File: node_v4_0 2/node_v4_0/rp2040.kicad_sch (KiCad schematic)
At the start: 29 parts, among them U1 RP2040, U2 W25Q128JVS, U7 PTS526 SK15 SMTR2 LFS, U8 PTS526 SK15 SMTR2 LFS

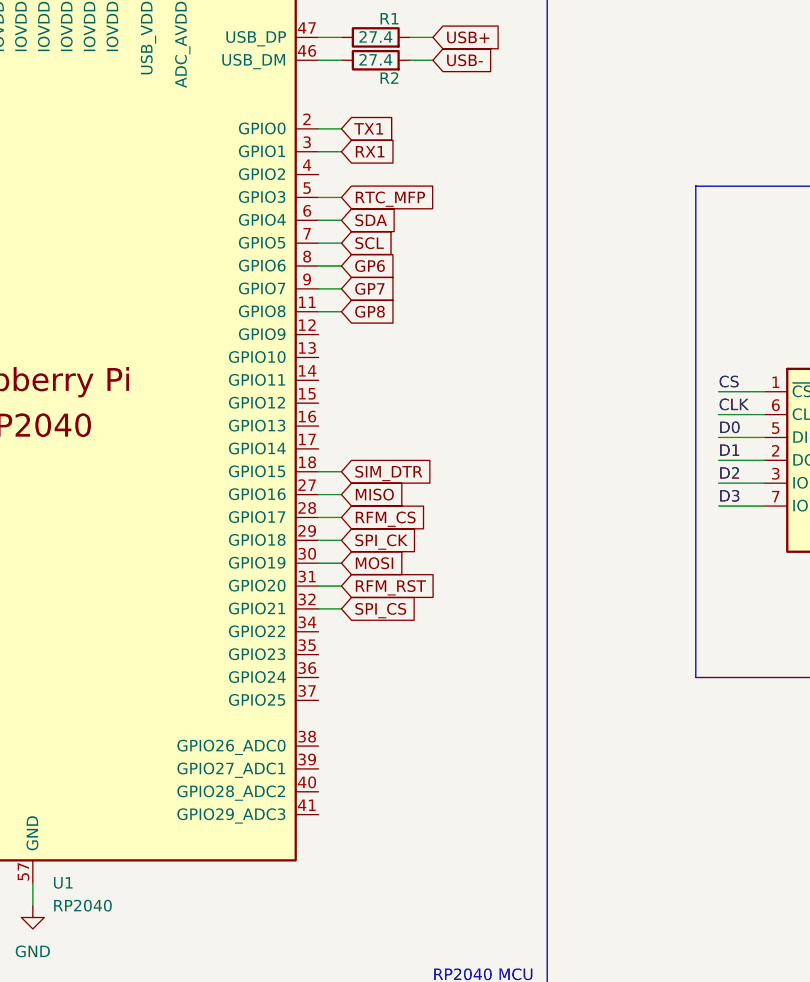
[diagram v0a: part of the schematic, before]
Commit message: finished laying out the board
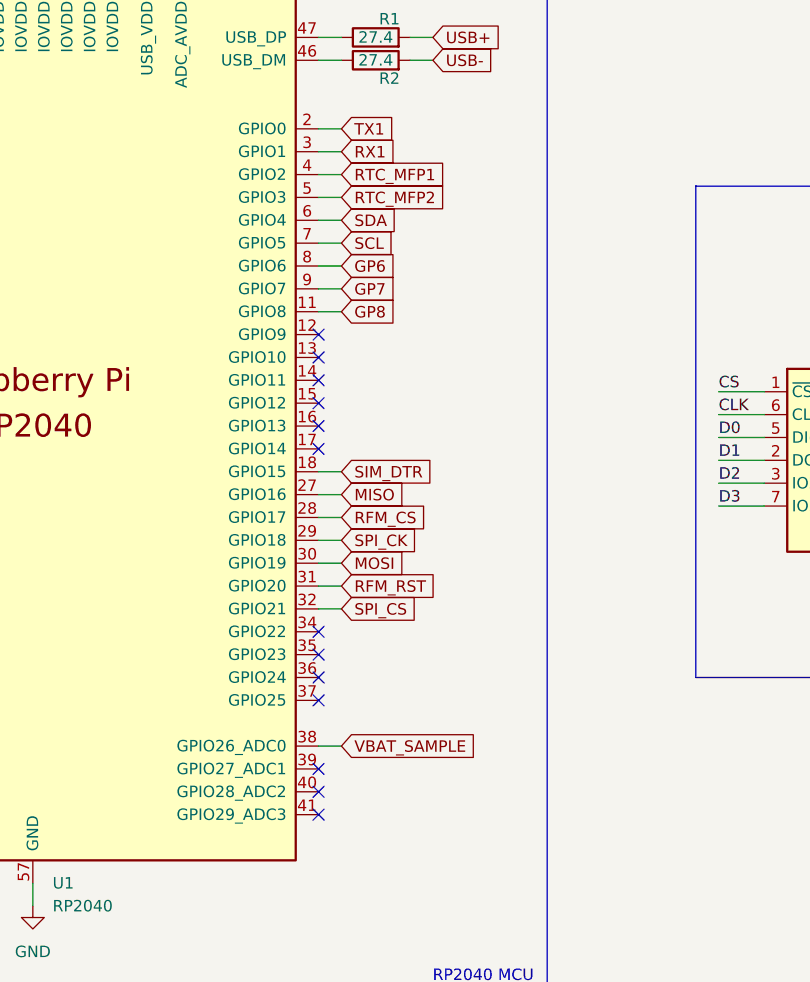
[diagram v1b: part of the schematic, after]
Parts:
- U7, U8: footprint pts526:SMT_FS -> WiSDOM:PTS526
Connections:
- net VBAT_SAMPLE: now reaches U1.38 (GPIO26_ADC0)
- net RTC_MFP1: now reaches U1.4 (GPIO2)
- net RTC_MFP renamed RTC_MFP2
- no-connect marks 0 -> 13
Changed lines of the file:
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@@
 		(color 0 0 0 0)
 	)
+	(no_connect
+		(at 95.25 133.35)
+	)
+	(no_connect
+		(at 95.25 130.81)
+	)
+	(no_connect
+		(at 95.25 135.89)
+	)
+	(no_connect
+		(at 95.25 125.73)
+	)
+	(no_connect
+		(at 95.25 173.99)
+	)
+	(no_connect
+		(at 95.25 128.27)
+	)
+	(no_connect
+		(at 95.25 156.21)
+	)
+	(no_connect
+		(at 95.25 161.29)
+	)
+	(no_connect
+		(at 95.25 163.83)
+	)
+	(no_connect
+		(at 95.25 176.53)
+	)
+	(no_connect
+		(at 95.25 158.75)
+	)
+	(no_connect
+		(at 95.25 123.19)
+	)
+	(no_connect
+		(at 95.25 171.45)
+	)
 	(wire
 		(pts
@@
 	(wire
 		(pts
+			(xy 95.25 168.91) (xy 97.79 168.91)
+		)
+		(stroke
+			(width 0)
+			(type default)
+		)
+	)
+	(wire
+		(pts
 			(xy 27.94 25.4) (xy 40.64 25.4)
 		)
@@
 	(wire
 		(pts
+			(xy 95.25 105.41) (xy 97.79 105.41)
+		)
+		(stroke
+			(width 0)
+			(type default)
+		)
+	)
+	(wire
+		(pts
 			(xy 180.34 40.64) (xy 180.34 41.91)
 		)
@@
 		)
 	)
-	(global_label "RTC_MFP"
+	(global_label "RTC_MFP2"
 		(shape input)
 		(at 97.79 107.95 0)
@@
 		)
 		(property "Intersheetrefs" "${INTERSHEET_REFS}"
-			(at 109.0604 107.95 0)
+			(at 110.2699 107.95 0)
+			(effects
+				(font
+					(size 1.27 1.27)
+				)
+				(justify left)
+				(hide yes)
+			)
+		)
+	)
+	(global_label "RTC_MFP1"
+		(shape input)
+		(at 97.79 105.41 0)
+		(fields_autoplaced yes)
+		(effects
+			(font
+				(size 1.27 1.27)
+			)
+			(justify left)
+		)
+		(property "Intersheetrefs" "${INTERSHEET_REFS}"
+			(at 110.2699 105.41 0)
 			(effects
 				(font
@@
 		)
 	)
+	(global_label "VBAT_SAMPLE"
+		(shape input)
+		(at 97.79 168.91 0)
+		(fields_autoplaced yes)
+		(effects
+			(font
+				(size 1.27 1.27)
+			)
+			(justify left)
+		)
+		(property "Intersheetrefs" "${INTERSHEET_REFS}"
+			(at 113.3542 168.91 0)
+			(effects
+				(font
+					(size 1.27 1.27)
+				)
+				(justify left)
+				(hide yes)
+			)
+		)
+	)
 	(global_label "MOSI"
 		(shape input)
@@
 			)
 		)
-		(property "Footprint" "pts526:SMT_FS"
+		(property "Footprint" "WiSDOM:PTS526"
 			(at 233.68 85.852 0)
 			(effects
@@
 			)
 		)
-		(property "Footprint" "pts526:SMT_FS"
+		(property "Footprint" "WiSDOM:PTS526"
 			(at 232.41 106.172 0)
 			(effects

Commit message: most routing done
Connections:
- net GP27: now reaches U1.39 (GPIO27_ADC1)
- net GP28: now reaches U1.40 (GPIO28_ADC2)
- net GP29: now reaches U1.41 (GPIO29_ADC3)
- net GP6: no longer names the net of U1.8 (GPIO6)
- net GP7: no longer names the net of U1.9 (GPIO7)
- net GP8: no longer names the net of U1.11 (GPIO8)
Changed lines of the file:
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@@
+	)
+	(no_connect
+		(at 95.25 120.65)
+	)
+	(no_connect
+		(at 95.25 115.57)
 	)
 	(no_connect
@@
 	)
 	(no_connect
-		(at 95.25 173.99)
-	)
-	(no_connect
 		(at 95.25 128.27)
 	)
@@
 	)
 	(no_connect
-		(at 95.25 176.53)
+		(at 95.25 118.11)
 	)
 	(no_connect
@@
 		(at 95.25 123.19)
 	)
-	(no_connect
-		(at 95.25 171.45)
-	)
 	(wire
 		(pts
@@
 	(wire
 		(pts
-			(xy 95.25 115.57) (xy 97.79 115.57)
-		)
-		(stroke
-			(width 0)
-			(type default)
-		)
-	)
-	(wire
-		(pts
 			(xy 59.69 76.2) (xy 59.69 82.55)
 		)
@@
 	(wire
 		(pts
-			(xy 95.25 120.65) (xy 97.79 120.65)
-		)
-		(stroke
-			(width 0)
-			(type default)
-		)
-	)
-	(wire
-		(pts
 			(xy 95.25 107.95) (xy 97.79 107.95)
 		)
@@
 	(wire
 		(pts
-			(xy 95.25 118.11) (xy 97.79 118.11)
-		)
-		(stroke
-			(width 0)
-			(type default)
-		)
-	)
-	(wire
-		(pts
 			(xy 173.99 127) (xy 173.99 128.27)
 		)
@@
 	(wire
 		(pts
+			(xy 95.25 176.53) (xy 97.79 176.53)
+		)
+		(stroke
+			(width 0)
+			(type default)
+		)
+	)
+	(wire
+		(pts
 			(xy 173.99 118.11) (xy 186.69 118.11)
 		)
@@
 	(wire
 		(pts
+			(xy 95.25 171.45) (xy 97.79 171.45)
+		)
+		(stroke
+			(width 0)
+			(type default)
+		)
+	)
+	(wire
+		(pts
 			(xy 80.01 76.2) (xy 80.01 82.55)
 		)
@@
 		(pts
 			(xy 233.68 33.02) (xy 233.68 31.75)
+		)
+		(stroke
+			(width 0)
+			(type default)
+		)
+	)
+	(wire
+		(pts
+			(xy 95.25 173.99) (xy 97.79 173.99)
 		)
 		(stroke
@@
 		)
 	)
-	(global_label "GP8"
-		(shape input)
-		(at 97.79 120.65 0)
-		(fields_autoplaced yes)
-		(effects
-			(font
-				(size 1.27 1.27)
-			)
-			(justify left)
-		)
-		(property "Intersheetrefs" "${INTERSHEET_REFS}"
-			(at 104.5247 120.65 0)
-			(effects
-				(font
-					(size 1.27 1.27)
-				)
-				(justify left)
-				(hide yes)
-			)
-		)
-	)
 	(global_label "SDA"
 		(shape input)
@@
 		)
 	)
-	(global_label "GP7"
-		(shape input)
-		(at 97.79 118.11 0)
-		(fields_autoplaced yes)
-		(effects
-			(font
-				(size 1.27 1.27)
-			)
-			(justify left)
-		)
-		(property "Intersheetrefs" "${INTERSHEET_REFS}"
-			(at 104.5247 118.11 0)
-			(effects
-				(font
-					(size 1.27 1.27)
-				)
-				(justify left)
-				(hide yes)
-			)
-		)
-	)
 	(global_label "TX1"
 		(shape input)
@@
 		)
 	)
-	(global_label "GP6"
-		(shape input)
-		(at 97.79 115.57 0)
-		(fields_autoplaced yes)
-		(effects
-			(font
-				(size 1.27 1.27)
-			)
-			(justify left)
-		)
-		(property "Intersheetrefs" "${INTERSHEET_REFS}"
-			(at 104.5247 115.57 0)
-			(effects
-				(font
-					(size 1.27 1.27)
-				)
-				(justify left)
-				(hide yes)
-			)
-		)
-	)
 	(global_label "SWCLK"
 		(shape input)
@@
 		)
 	)
+	(global_label "GP28"
+		(shape input)
+		(at 97.79 173.99 0)
+		(fields_autoplaced yes)
+		(effects
+			(font
+				(size 1.27 1.27)
+			)
+			(justify left)
+		)
+		(property "Intersheetrefs" "${INTERSHEET_REFS}"
+			(at 105.7342 173.99 0)
+			(effects
+				(font
+					(size 1.27 1.27)
+				)
+				(justify left)
+				(hide yes)
+			)
+		)
+	)
 	(global_label "RFM_CS"
 		(shape input)
@@
 		)
 	)
+	(global_label "GP29"
+		(shape input)
+		(at 97.79 176.53 0)
+		(fields_autoplaced yes)
+		(effects
+			(font
+				(size 1.27 1.27)
+			)
+			(justify left)
+		)
+		(property "Intersheetrefs" "${INTERSHEET_REFS}"
+			(at 105.7342 176.53 0)
+			(effects
+				(font
+					(size 1.27 1.27)
+				)
+				(justify left)
+				(hide yes)
+			)
+		)
+	)
 	(global_label "VBAT_SAMPLE"
 		(shape input)
@@
 			(effects
 				(font
+					(size 1.27 1.27)
+				)
+				(justify left)
+				(hide yes)
+			)
+		)
+	)
+	(global_label "GP27"
+		(shape input)
+		(at 97.79 171.45 0)
+		(fields_autoplaced yes)
+		(effects
+			(font
+				(size 1.27 1.27)
+			)
+			(justify left)
+		)
+		(property "Intersheetrefs" "${INTERSHEET_REFS}"
+			(at 105.7342 171.45 0)
+			(effects
+				(font

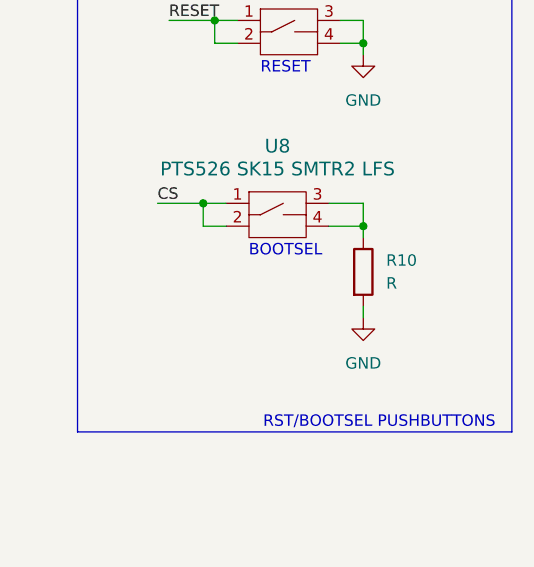
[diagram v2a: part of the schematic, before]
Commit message: moved reset button to make space for vin jst connector
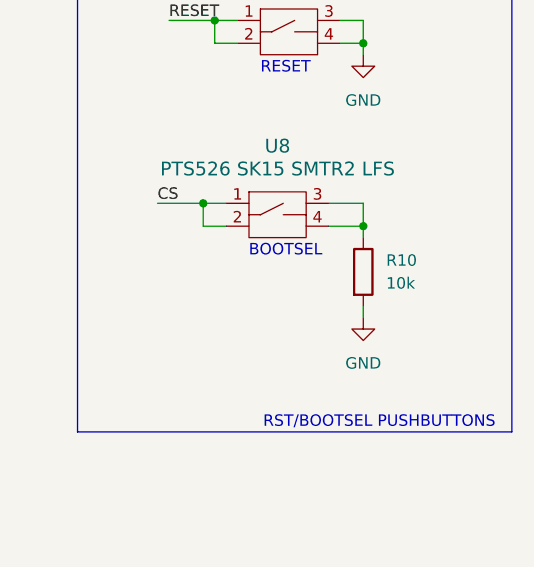
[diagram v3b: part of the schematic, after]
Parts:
- R10: value R -> 10k
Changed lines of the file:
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@@
 			)
 		)
-		(property "Value" "R"
+		(property "Value" "10k"
 			(at 245.11 120.6499 0)
 			(effects
